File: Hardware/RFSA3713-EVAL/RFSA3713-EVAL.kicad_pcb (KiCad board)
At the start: 2 copper layers, 53.9 x 45.5 mm, 17 parts, among them J1 Conn_Coaxial, J2 Conn_Coaxial, J4 Conn_Coaxial, J5 Conn_Coaxial, J6 Conn_02x05_Odd_Even, SW1 SW_SPDT, SW2 SW_SPDT, SW3 SW_SPDT

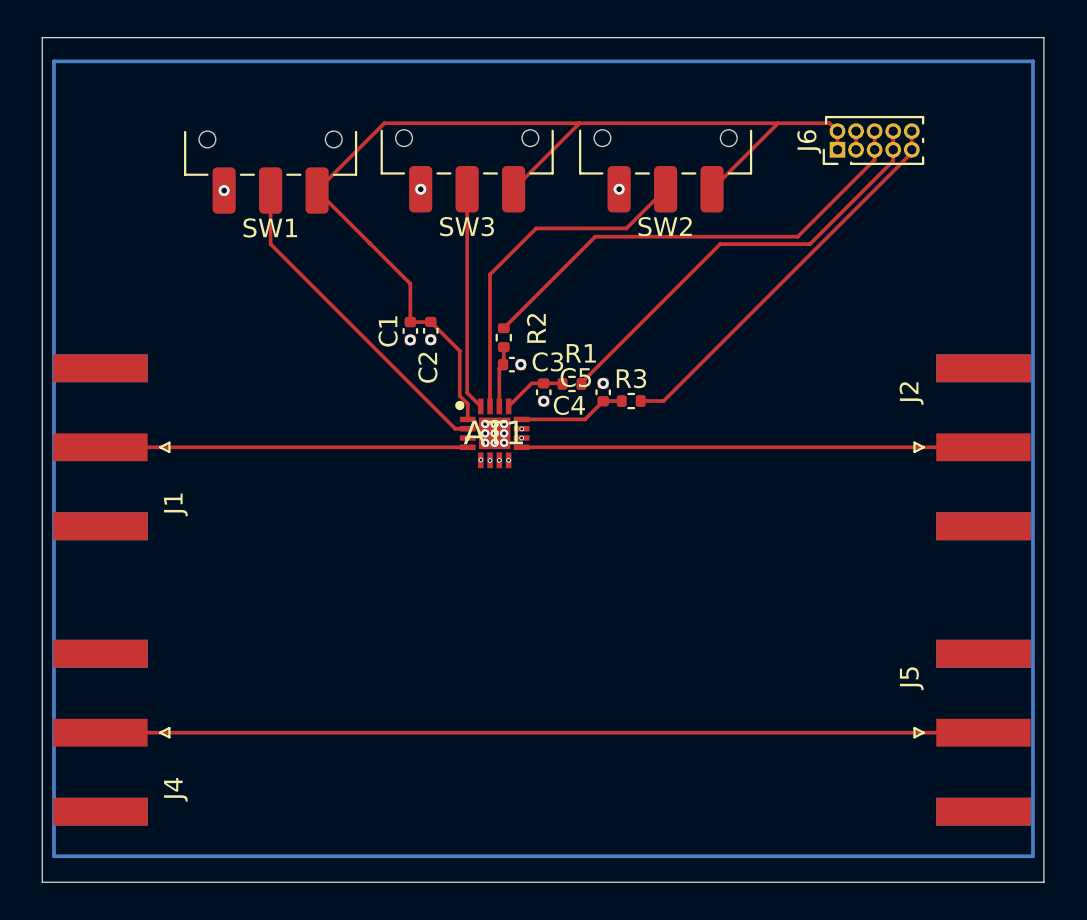
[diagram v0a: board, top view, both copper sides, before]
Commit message: Added Waveguides
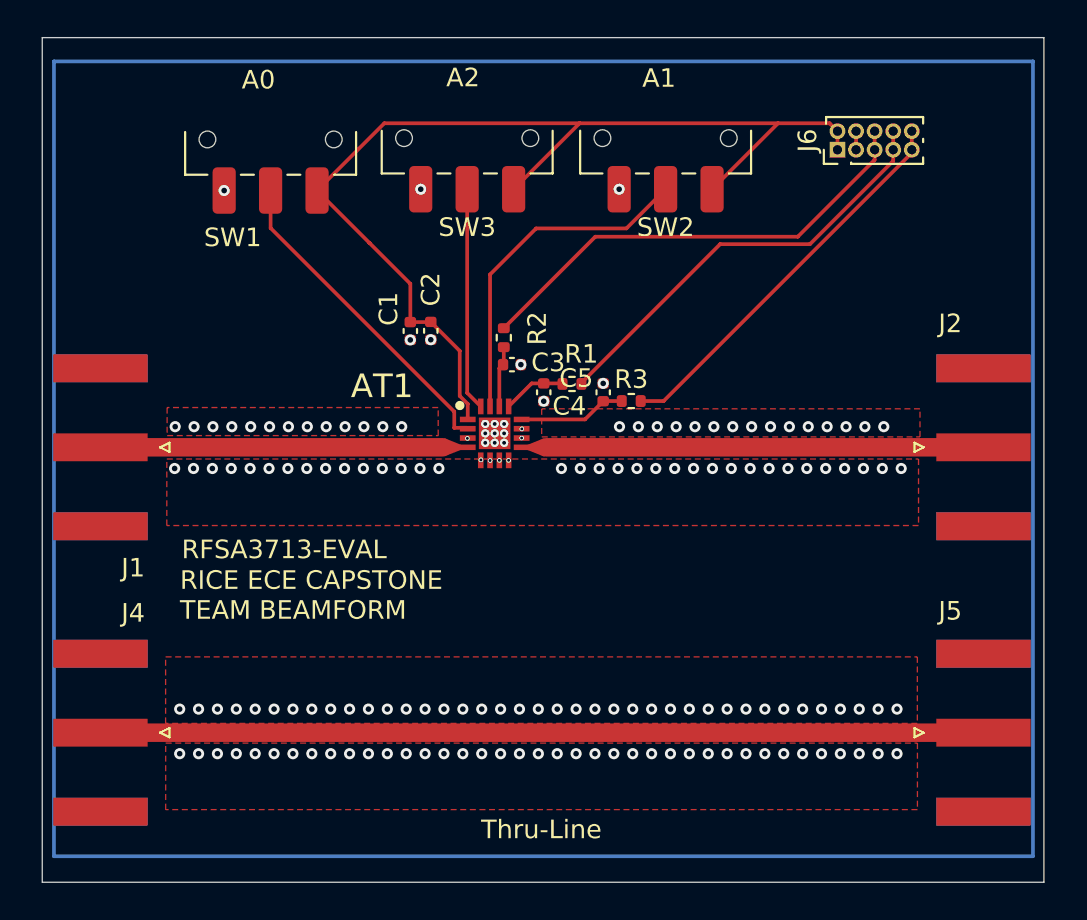
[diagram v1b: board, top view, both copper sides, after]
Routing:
- net Net-(AT1-RFOUT): track 24.9 -> 23.6 mm
- net GND: vias 24 -> 164
- added copper zone on F.Cu, net GND
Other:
- board text added: "A0"
- board text added: "A1"
- board text added: "A2"
- board text added: "RFSA3713-EVAL"
- board text added: "RICE ECE CAPSTONE TEAM BEAMFORM"
- board text added: "Thru-Line"

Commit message: fixed attenuator board to fit DRC
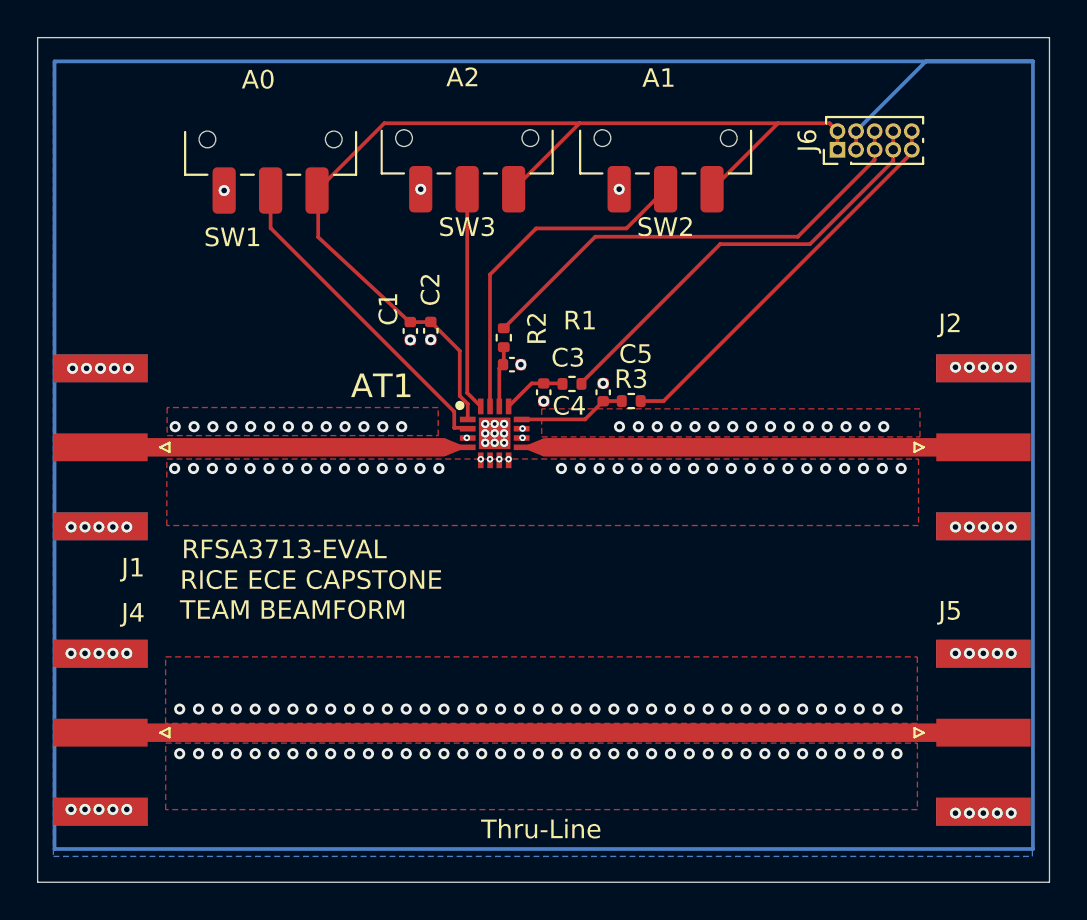
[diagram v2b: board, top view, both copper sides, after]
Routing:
- net GND: track 1.00 -> 12.1 mm, vias 164 -> 204
- net VDD: track 57.1 -> 47.9 mm
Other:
- board size 53.9 x 45.5 mm -> 54.5 x 45.5 mm

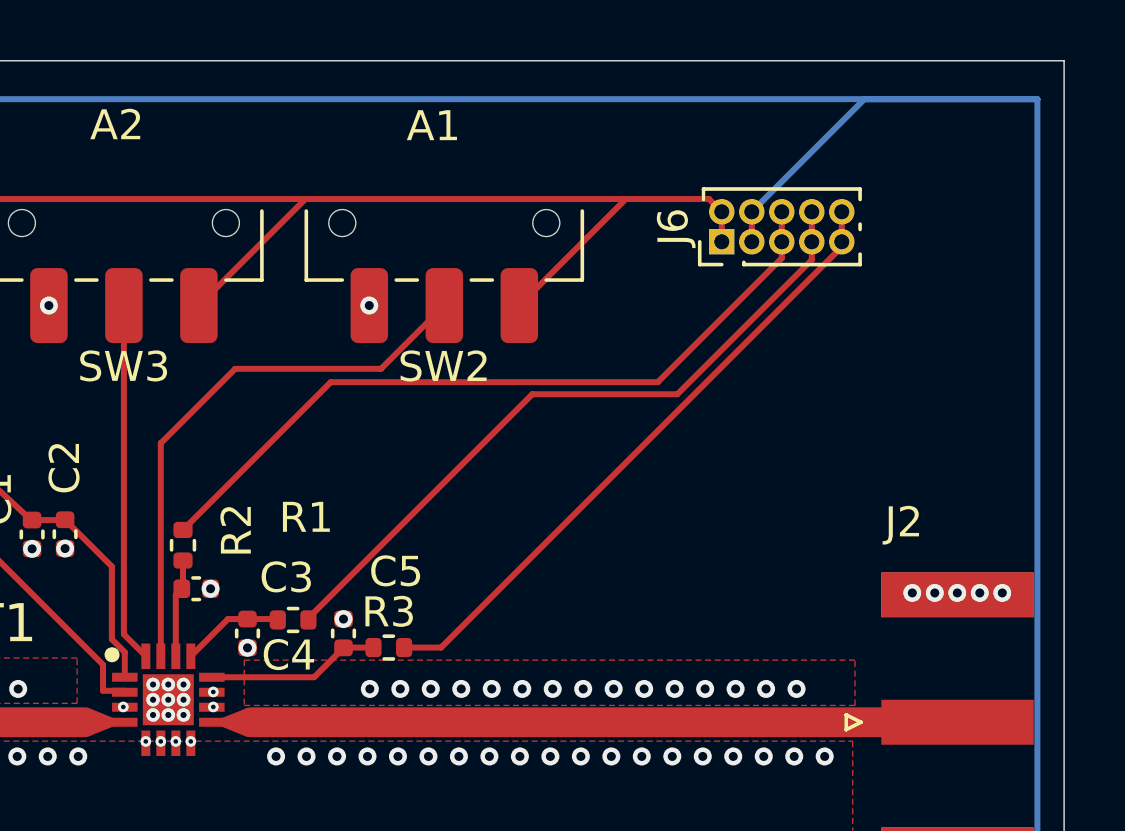
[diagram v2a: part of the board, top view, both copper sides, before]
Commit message: DRC and header re-sizing
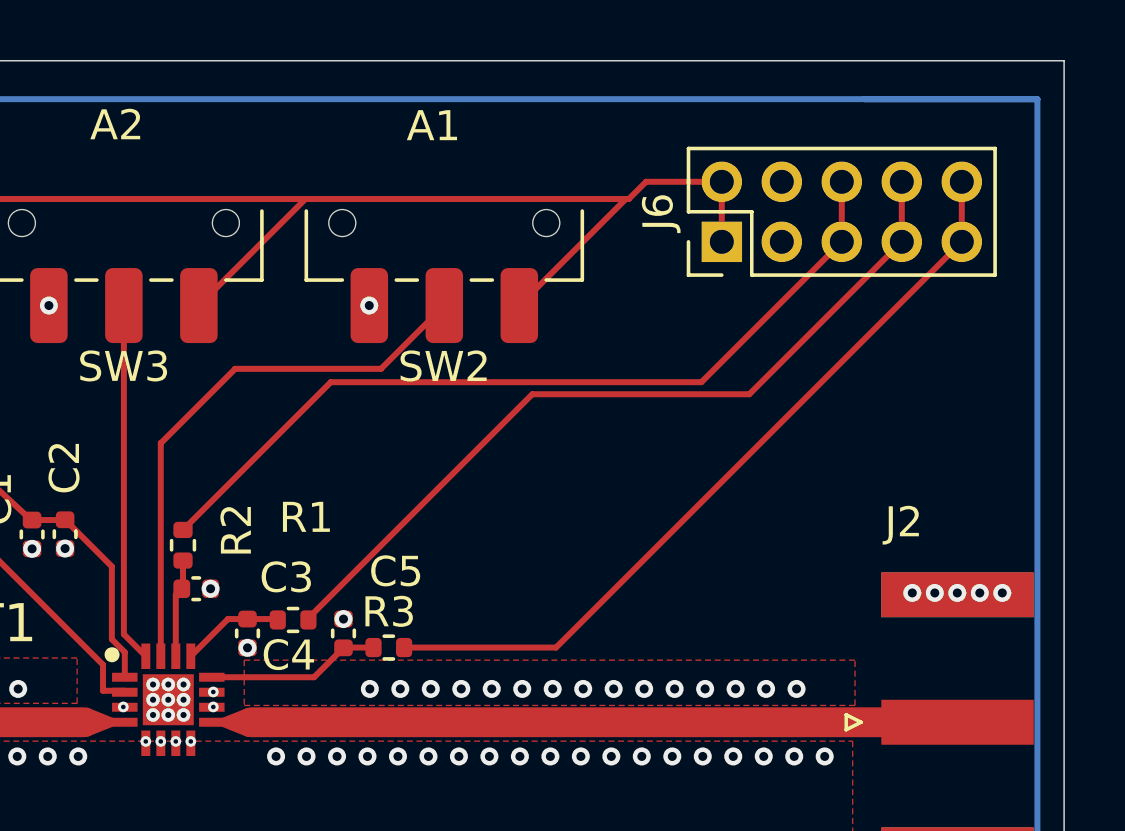
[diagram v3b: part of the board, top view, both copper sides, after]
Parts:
- J6: footprint Connector_PinHeader_1.00mm:PinHeader_2x05_P1.00mm_Vertical -> Connector_PinHeader_2.00mm:PinHeader_2x05_P2.00mm_Vertical
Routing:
- net GND: track 12.1 -> 6.31 mm
- net LE: track 21.3 -> 26.2 mm
- net CLK: track 23.4 -> 27.1 mm
- net SI: track 25.3 -> 28.1 mm
- net VDD: track 47.9 -> 49.0 mm

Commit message: Fixed JLCPCB Errors
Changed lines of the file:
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@@
 			(plot_on_all_layers_selection 0x00000000_00000000_00000000_00000000)
 			(disableapertmacros no)
-			(usegerberextensions no)
+			(usegerberextensions yes)
 			(usegerberattributes yes)
 			(usegerberadvancedattributes yes)
@@
 			(sketchdnponfab yes)
 			(crossoutdnponfab yes)
-			(subtractmaskfromsilk no)
+			(subtractmaskfromsilk yes)
 			(outputformat 1)
 			(mirror no)
-			(drillshape 1)
+			(drillshape 0)
 			(scaleselection 1)
-			(outputdirectory "")
+			(outputdirectory "NoCutTest/")
 		)
 	)
@@
 	(via
 		(at 197.55 62.55)
-		(size 0.3556)
-		(drill 0.1524)
+		(size 0.45)
+		(drill 0.2)
 		(layers "F.Cu" "B.Cu")
 		(teardrops
@@
 	(via
 		(at 198.55 62.55)
-		(size 0.3556)
-		(drill 0.1524)
+		(size 0.45)
+		(drill 0.2)
 		(layers "F.Cu" "B.Cu")
 		(teardrops
@@
 	(via
 		(at 199.8 61.4)
-		(size 0.3556)
-		(drill 0.1524)
+		(size 0.45)
+		(drill 0.2)
 		(layers "F.Cu" "B.Cu")
 		(teardrops
@@
 	(via
 		(at 196.8 61.4)
-		(size 0.3556)
-		(drill 0.1524)
+		(size 0.45)
+		(drill 0.2)
 		(layers "F.Cu" "B.Cu")
 		(teardrops
@@
 	(via
 		(at 198.05 62.55)
-		(size 0.3556)
-		(drill 0.1524)
+		(size 0.45)
+		(drill 0.2)
 		(layers "F.Cu" "B.Cu")
 		(teardrops
@@
 	(via
 		(at 199.05 62.55)
-		(size 0.3556)
-		(drill 0.1524)
+		(size 0.45)
+		(drill 0.2)
 		(layers "F.Cu" "B.Cu")
 		(teardrops
@@
 	(via
 		(at 199.8 60.9)
-		(size 0.3556)
-		(drill 0.1524)
+		(size 0.45)
+		(drill 0.2)
 		(layers "F.Cu" "B.Cu")
 		(teardrops
@@
 	)
 	(segment
-		(start 198.75 57.46)
-		(end 198.55 57.66)
+		(start 198.79 56.52)
+		(end 198.79 57.42)
 		(width 0.2)
 		(layer "F.Cu")
@@
 	)
 	(segment
-		(start 198.79 56.52)
-		(end 198.79 57.42)
+		(start 198.55 59.71)
+		(end 198.55 57.66)
 		(width 0.2)
 		(layer "F.Cu")
@@
 	(segment
 		(start 198.55 57.66)
-		(end 198.55 59.71)
+		(end 198.75 57.46)
 		(width 0.2)
 		(layer "F.Cu")
